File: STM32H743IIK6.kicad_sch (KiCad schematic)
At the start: 57 parts, among them J4 USB-C, J6 BAT, SW1 SW_Push, SW2 SW_Push, SW3 SW_Push, SW4 SW_Push, U4 STM32H723ZGTx, U8 TLV75733PDBV, Y1 25MHz, Y2 32.768KHz

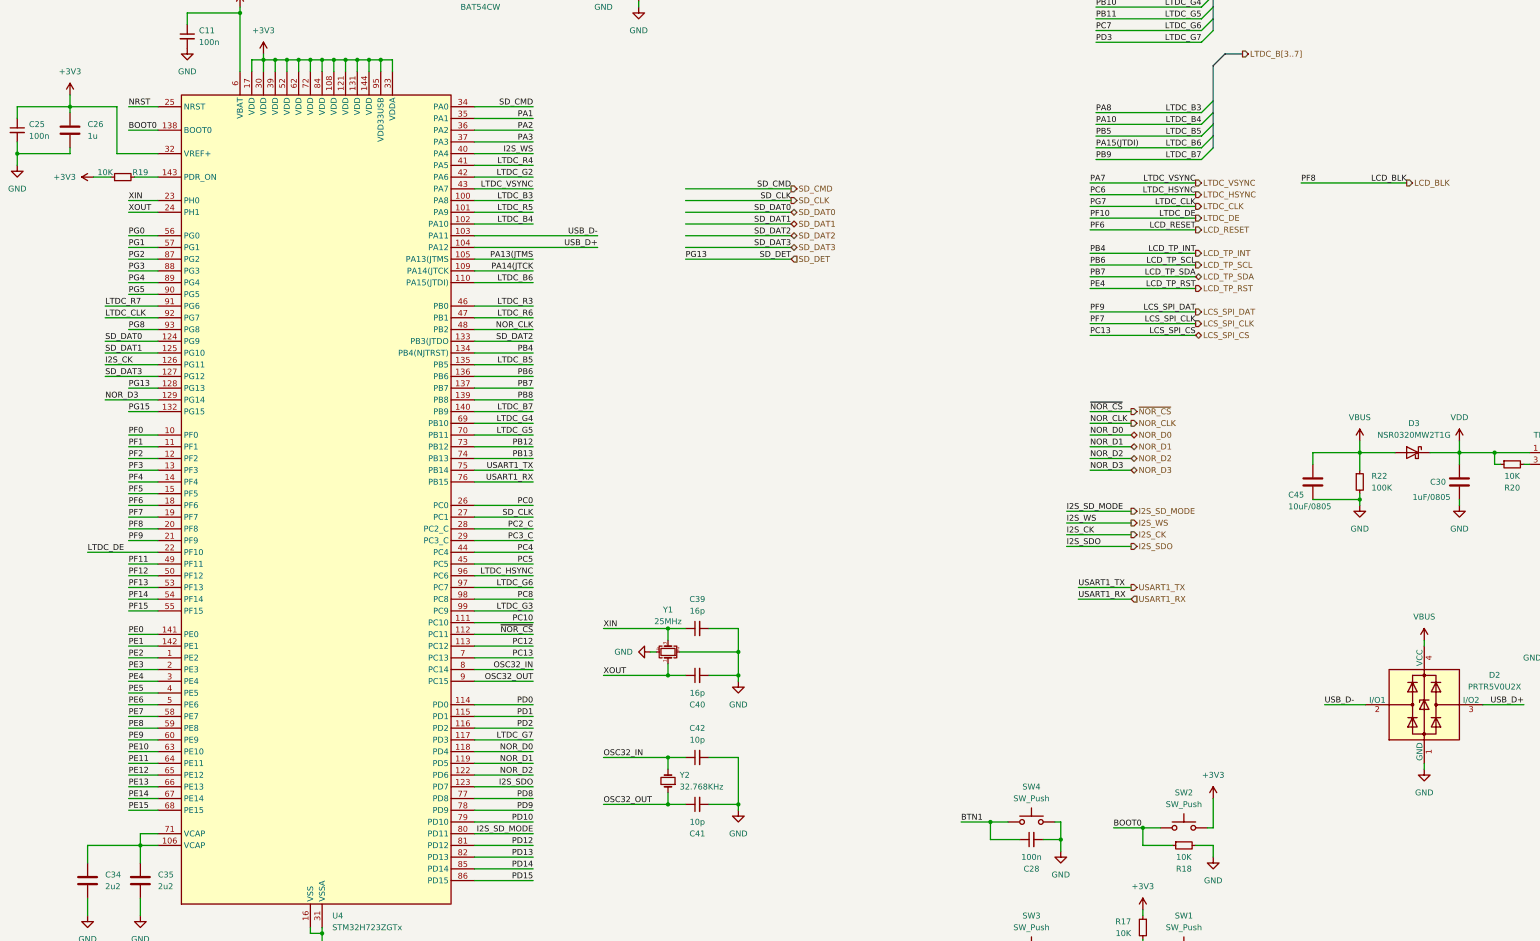
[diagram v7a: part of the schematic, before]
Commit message: All clear (need to verify). LCD backlight driver left untracked
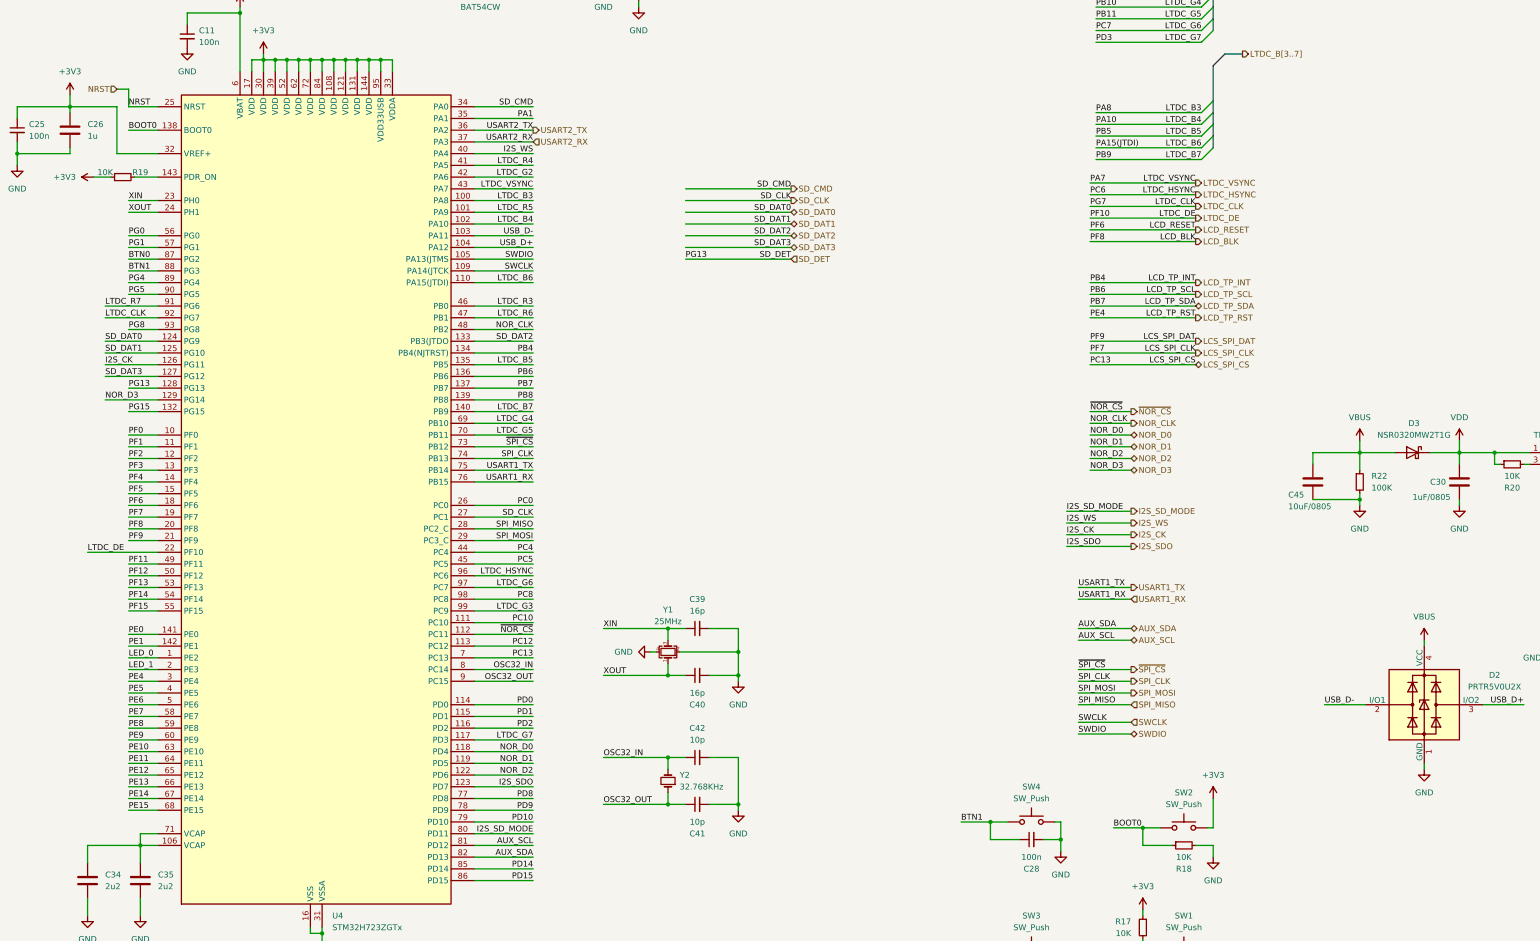
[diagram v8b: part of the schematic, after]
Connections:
- net PE2 is gone; now on net LED_0: U4.1 (PE2)
- net PE3 is gone; now on net LED_1: U4.2 (PE3)
- net PG2 is gone; now on net BTN0: U4.87 (PG2)
- net PG3 is gone; now on net BTN1: U4.88 (PG3)
- net PA13(JTMS renamed SWDIO
- net PA14(JTCK renamed SWCLK
- net PA2 renamed USART2_TX
- net PA3 renamed USART2_RX
- net PB12 renamed ~{SPI_CS}
- net PB13 renamed SPI_CLK
- net PC2_C renamed SPI_MISO
- net PC3_C renamed SPI_MOSI
- net PD12 renamed AUX_SCL
- net PD13 renamed AUX_SDA
